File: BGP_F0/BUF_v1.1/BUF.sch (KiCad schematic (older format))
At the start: 34 parts, among them P1 CONN_01X02, P2 CONN_01X02, P3 CONN_01X03, P4 CONN_01X02, P5 Conn_01x06, P6 Conn_01x05, P7 CONN_01X02, Q1 2N5457, Q2 2N5457, U1 MC33178

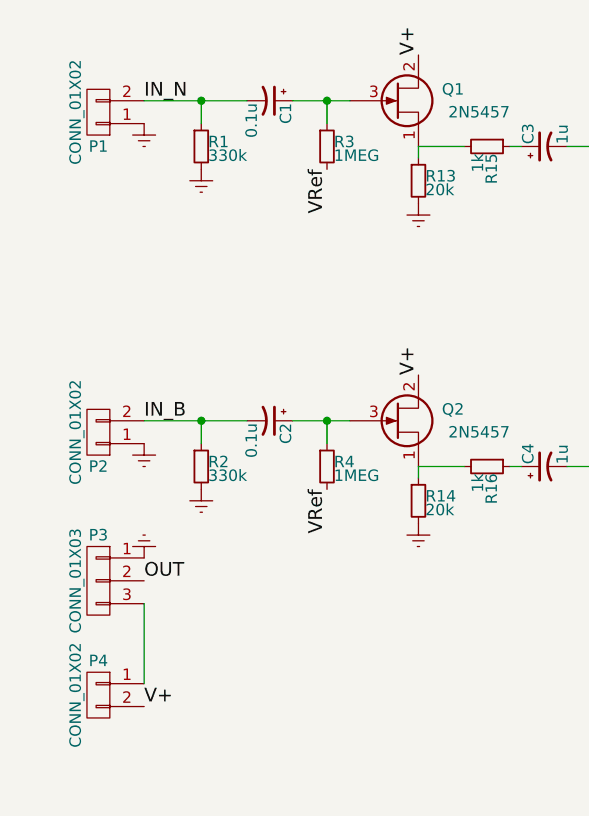
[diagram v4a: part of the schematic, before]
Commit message: F0 - BUF JFET bypass caps at i/p
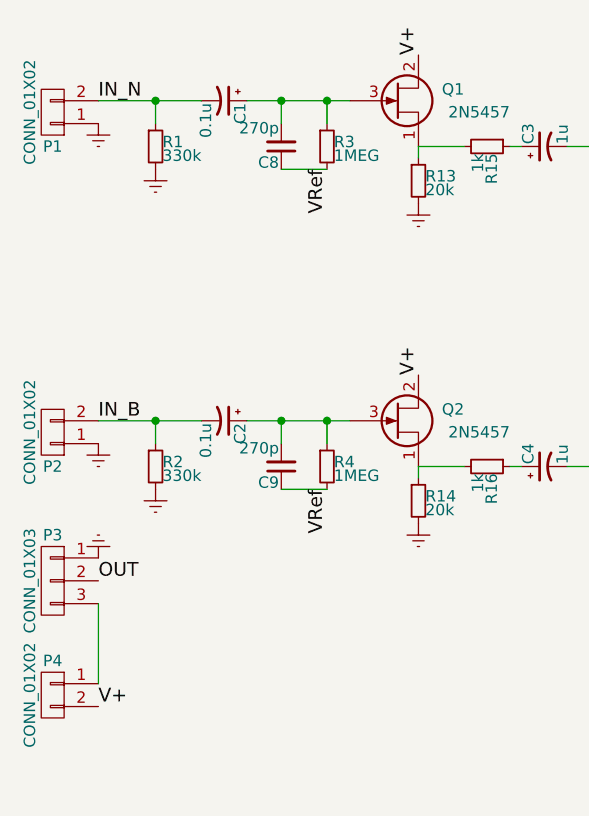
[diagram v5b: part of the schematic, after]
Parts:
- added C8, C9: 270p, Capacitors_SMD:C_0603, symbol C_Small
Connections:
- net VRef: now also C8.1, C9.1
- net at C1.1, Q1.3 (G), R3.1: now also C8.2
- net at C2.1, Q2.3 (G), R4.1: now also C9.2
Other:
- moved on the sheet: C1, C2, P1, P2, P3, P4, R1, R2
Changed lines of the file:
@@
 L R_Small R1
 U 1 1 5A65126F
-P 2850 2700
-F 0 "R1" H 2880 2720 50  0000 L CNN
-F 1 "330k" H 2880 2660 50  0000 L CNN
-F 2 "Resistors_SMD:R_0603" H 2850 2700 50  0001 C CNN
-F 3 "" H 2850 2700 50  0000 C CNN
-	1    2850 2700
+P 2650 2700
+F 0 "R1" H 2680 2720 50  0000 L CNN
+F 1 "330k" H 2680 2660 50  0000 L CNN
+F 2 "Resistors_SMD:R_0603" H 2650 2700 50  0001 C CNN
+F 3 "" H 2650 2700 50  0000 C CNN
+	1    2650 2700
 	1    0    0    -1
 $EndComp
@@
 L Earth #PWR01
 U 1 1 5A651373
-P 2850 2800
-F 0 "#PWR01" H 2850 2550 50  0001 C CNN
-F 1 "Earth" H 2850 2650 50  0001 C CNN
-F 2 "" H 2850 2800 50  0000 C CNN
-F 3 "" H 2850 2800 50  0000 C CNN
-	1    2850 2800
+P 2650 2800
+F 0 "#PWR01" H 2650 2550 50  0001 C CNN
+F 1 "Earth" H 2650 2650 50  0001 C CNN
+F 2 "" H 2650 2800 50  0000 C CNN
+F 3 "" H 2650 2800 50  0000 C CNN
+	1    2650 2800
 	1    0    0    -1
 $EndComp
@@
 L R_Small R2
 U 1 1 5A653A92
-P 2850 4100
-F 0 "R2" H 2880 4120 50  0000 L CNN
-F 1 "330k" H 2880 4060 50  0000 L CNN
-F 2 "Resistors_SMD:R_0603" H 2850 4100 50  0001 C CNN
-F 3 "" H 2850 4100 50  0000 C CNN
-	1    2850 4100
+P 2650 4100
+F 0 "R2" H 2680 4120 50  0000 L CNN
+F 1 "330k" H 2680 4060 50  0000 L CNN
+F 2 "Resistors_SMD:R_0603" H 2650 4100 50  0001 C CNN
+F 3 "" H 2650 4100 50  0000 C CNN
+	1    2650 4100
 	1    0    0    -1
 $EndComp
@@
 Text Label 6400 3300 0    60   ~ 0
 IN_EQ
-Text Label 2600 3900 0    60   ~ 0
+Text Label 2400 3900 0    60   ~ 0
 IN_B
 Text Label 8350 3550 2    60   ~ 0
@@
 Text Label 8350 4600 2    60   ~ 0
 V+
-Text Label 2600 5150 0    60   ~ 0
+Text Label 2400 5150 0    60   ~ 0
 V+
-Text Label 2600 4600 0    60   ~ 0
+Text Label 2400 4600 0    60   ~ 0
 OUT
 $Comp
 L Earth #PWR07
 U 1 1 5A658545
-P 2600 4000
-F 0 "#PWR07" H 2600 3750 50  0001 C CNN
-F 1 "Earth" H 2600 3850 50  0001 C CNN
-F 2 "" H 2600 4000 50  0000 C CNN
-F 3 "" H 2600 4000 50  0000 C CNN
-	1    2600 4000
+P 2400 4000
+F 0 "#PWR07" H 2400 3750 50  0001 C CNN
+F 1 "Earth" H 2400 3850 50  0001 C CNN
+F 2 "" H 2400 4000 50  0000 C CNN
+F 3 "" H 2400 4000 50  0000 C CNN
+	1    2400 4000
 	1    0    0    -1
 $EndComp
@@
 L Earth #PWR08
 U 1 1 5A6585B9
-P 2600 2600
-F 0 "#PWR08" H 2600 2350 50  0001 C CNN
-F 1 "Earth" H 2600 2450 50  0001 C CNN
-F 2 "" H 2600 2600 50  0000 C CNN
-F 3 "" H 2600 2600 50  0000 C CNN
-	1    2600 2600
-	1    0    0    -1
-$EndComp
-Text Label 2600 2500 0    60   ~ 0
+P 2400 2600
+F 0 "#PWR08" H 2400 2350 50  0001 C CNN
+F 1 "Earth" H 2400 2450 50  0001 C CNN
+F 2 "" H 2400 2600 50  0000 C CNN
+F 3 "" H 2400 2600 50  0000 C CNN
+	1    2400 2600
+	1    0    0    -1
+$EndComp
+Text Label 2400 2500 0    60   ~ 0
 IN_N
 Text Label 6100 5100 0    60   ~ 0
@@
 Wire Wire Line
 	4850 5150 4850 4800
-Connection ~ 2850 3900
-Connection ~ 2850 2500
-Wire Wire Line
-	2600 5050 2600 4700
+Connection ~ 2650 3900
+Connection ~ 2650 2500
+Wire Wire Line
+	2400 5050 2400 4700
 Wire Wire Line
 	7100 3300 6750 3300
@@
 	3800 4150 3800 4100
 Wire Wire Line
-	2850 3900 2850 4000
-Wire Wire Line
-	2600 3900 3050 3900
+	2650 3900 2650 4000
+Wire Wire Line
+	2400 3900 2850 3900
 Connection ~ 3400 3900
 Wire Wire Line
 	3400 3900 3400 4000
 Wire Wire Line
-	2850 2500 2850 2600
-Wire Wire Line
-	2600 2500 3050 2500
+	2650 2500 2650 2600
+Wire Wire Line
+	2400 2500 2850 2500
 Connection ~ 3400 2500
 Wire Wire Line
@@
 	3800 2750 3800 2700
 Wire Wire Line
-	3500 2500 3250 2500
-Wire Wire Line
-	3500 3900 3250 3900
+	3050 2500 3500 2500
+Wire Wire Line
+	3050 3900 3500 3900
 $Comp
 L Earth #PWR010
 U 1 1 5A65837A
-P 2600 4500
-F 0 "#PWR010" H 2600 4250 50  0001 C CNN
-F 1 "Earth" H 2600 4350 50  0001 C CNN
-F 2 "" H 2600 4500 50  0000 C CNN
-F 3 "" H 2600 4500 50  0000 C CNN
-	1    2600 4500
+P 2400 4500
+F 0 "#PWR010" H 2400 4250 50  0001 C CNN
+F 1 "Earth" H 2400 4350 50  0001 C CNN
+F 2 "" H 2400 4500 50  0000 C CNN
+F 3 "" H 2400 4500 50  0000 C CNN
+	1    2400 4500
 	-1   0    0    1
 $EndComp
@@
 L Earth #PWR011
 U 1 1 5A653A9E
-P 2850 4200
-F 0 "#PWR011" H 2850 3950 50  0001 C CNN
-F 1 "Earth" H 2850 4050 50  0001 C CNN
-F 2 "" H 2850 4200 50  0000 C CNN
-F 3 "" H 2850 4200 50  0000 C CNN
-	1    2850 4200
+P 2650 4200
+F 0 "#PWR011" H 2650 3950 50  0001 C CNN
+F 1 "Earth" H 2650 4050 50  0001 C CNN
+F 2 "" H 2650 4200 50  0000 C CNN
+F 3 "" H 2650 4200 50  0000 C CNN
+	1    2650 4200
 	1    0    0    -1
 $EndComp
@@
 L CP1_Small C1
 U 1 1 5A79331B
-P 3150 2500
-F 0 "C1" H 3160 2570 50  0000 L CNN
-F 1 "0.1u" H 3160 2420 50  0000 L CNN
-F 2 "Capacitors_Tantalum_SMD:TantalC_SizeR_EIA-2012" H 3150 2500 50  0001 C CNN
-F 3 "" H 3150 2500 50  0000 C CNN
-	1    3150 2500
+P 2950 2500
+F 0 "C1" H 2960 2570 50  0000 L CNN
+F 1 "0.1u" H 2960 2420 50  0000 L CNN
+F 2 "Capacitors_Tantalum_SMD:TantalC_SizeR_EIA-2012" H 2950 2500 50  0001 C CNN
+F 3 "" H 2950 2500 50  0000 C CNN
+	1    2950 2500
 	0    1    1    0
 $EndComp
@@
 L CP1_Small C2
 U 1 1 5A793406
-P 3150 3900
-F 0 "C2" H 3160 3970 50  0000 L CNN
-F 1 "0.1u" H 3160 3820 50  0000 L CNN
-F 2 "Capacitors_Tantalum_SMD:TantalC_SizeR_EIA-2012" H 3150 3900 50  0001 C CNN
-F 3 "" H 3150 3900 50  0000 C CNN
-	1    3150 3900
+P 2950 3900
+F 0 "C2" H 2960 3970 50  0000 L CNN
+F 1 "0.1u" H 2960 3820 50  0000 L CNN
+F 2 "Capacitors_Tantalum_SMD:TantalC_SizeR_EIA-2012" H 2950 3900 50  0001 C CNN
+F 3 "" H 2950 3900 50  0000 C CNN
+	1    2950 3900
 	0    1    1    0
 $EndComp
@@
 L CONN_01X03 P3
 U 1 1 5A657F5B
-P 2400 4600
-F 0 "P3" H 2400 4800 50  0000 C CNN
-F 1 "CONN_01X03" V 2500 4600 50  0000 C CNN
-F 2 "Terminal_Blocks:TerminalBlock_Pheonix_MPT-2.54mm_3pol" H 2400 4600 50  0001 C CNN
-F 3 "" H 2400 4600 50  0000 C CNN
-	1    2400 4600
+P 2200 4600
+F 0 "P3" H 2200 4800 50  0000 C CNN
+F 1 "CONN_01X03" V 2300 4600 50  0000 C CNN
+F 2 "Terminal_Blocks:TerminalBlock_Pheonix_MPT-2.54mm_3pol" H 2200 4600 50  0001 C CNN
+F 3 "" H 2200 4600 50  0000 C CNN
+	1    2200 4600
 	-1   0    0    -1
 $EndComp
@@
 L CONN_01X02 P4
 U 1 1 5A658137
-P 2400 5100
-F 0 "P4" H 2400 5250 50  0000 C CNN
-F 1 "CONN_01X02" V 2500 5100 50  0000 C CNN
-F 2 "Terminal_Blocks:TerminalBlock_Pheonix_MPT-2.54mm_2pol" H 2400 5100 50  0001 C CNN
-F 3 "" H 2400 5100 50  0000 C CNN
-	1    2400 5100
+P 2200 5100
+F 0 "P4" H 2200 5250 50  0000 C CNN
+F 1 "CONN_01X02" V 2300 5100 50  0000 C CNN
+F 2 "Terminal_Blocks:TerminalBlock_Pheonix_MPT-2.54mm_2pol" H 2200 5100 50  0001 C CNN
+F 3 "" H 2200 5100 50  0000 C CNN
+	1    2200 5100
 	-1   0    0    -1
 $EndComp
@@
 L CONN_01X02 P2
 U 1 1 5A656625
-P 2400 3950
-F 0 "P2" H 2400 4100 50  0000 C CNN
-F 1 "CONN_01X02" V 2500 3950 50  0000 C CNN
-F 2 "Terminal_Blocks:TerminalBlock_Pheonix_MPT-2.54mm_2pol" H 2400 3950 50  0001 C CNN
-F 3 "" H 2400 3950 50  0000 C CNN
-	1    2400 3950
+P 2200 3950
+F 0 "P2" H 2200 4100 50  0000 C CNN
+F 1 "CONN_01X02" V 2300 3950 50  0000 C CNN
+F 2 "Terminal_Blocks:TerminalBlock_Pheonix_MPT-2.54mm_2pol" H 2200 3950 50  0001 C CNN
+F 3 "" H 2200 3950 50  0000 C CNN
+	1    2200 3950
 	-1   0    0    1
 $EndComp
@@
 L CONN_01X02 P1
 U 1 1 5A65640A
-P 2400 2550
-F 0 "P1" H 2400 2700 50  0000 C CNN
-F 1 "CONN_01X02" V 2500 2550 50  0000 C CNN
-F 2 "Terminal_Blocks:TerminalBlock_Pheonix_MPT-2.54mm_2pol" H 2400 2550 50  0001 C CNN
-F 3 "" H 2400 2550 50  0000 C CNN
-	1    2400 2550
+P 2200 2550
+F 0 "P1" H 2200 2700 50  0000 C CNN
+F 1 "CONN_01X02" V 2300 2550 50  0000 C CNN
+F 2 "Terminal_Blocks:TerminalBlock_Pheonix_MPT-2.54mm_2pol" H 2200 2550 50  0001 C CNN
+F 3 "" H 2200 2550 50  0000 C CNN
+	1    2200 2550
 	-1   0    0    1
 $EndComp
@@
 	1    0    0    -1
 $EndComp
+$Comp
+L C_Small C8
+U 1 1 5AF7B3CC
+P 3200 2700
+F 0 "C8" H 3210 2770 50  0000 L CNN
+F 1 "270p" H 3210 2620 50  0000 L CNN
+F 2 "Capacitors_SMD:C_0603" H 3200 2700 50  0001 C CNN
+F 3 "" H 3200 2700 50  0000 C CNN
+	1    3200 2700
+	-1   0    0    1
+$EndComp
+$Comp
+L C_Small C9
+U 1 1 5AF7B618
+P 3200 4100
+F 0 "C9" H 3210 4170 50  0000 L CNN
+F 1 "270p" H 3210 4020 50  0000 L CNN
+F 2 "Capacitors_SMD:C_0603" H 3200 4100 50  0001 C CNN
+F 3 "" H 3200 4100 50  0000 C CNN
+	1    3200 4100
+	-1   0    0    1
+$EndComp
+Wire Wire Line
+	3200 4200 3400 4200
+Wire Wire Line
+	3200 4000 3200 3900
+Connection ~ 3200 3900
+Wire Wire Line
+	3200 2800 3400 2800
+Wire Wire Line
+	3200 2600 3200 2500
+Connection ~ 3200 2500
 $EndSCHEMATC

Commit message: Various
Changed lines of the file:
@@
 Text Label 7650 3300 0    60   ~ 0
 OUT
-Text Label 6400 3300 0    60   ~ 0
+Text Label 6650 3300 2    60   ~ 0
 IN_EQ
 Text Label 2400 3900 0    60   ~ 0

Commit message: Various
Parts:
- R5, R6: value 4.7k -> 100k
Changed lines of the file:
@@
 P 5200 2800
 F 0 "R5" H 5230 2820 50  0000 L CNN
-F 1 "4.7k" H 5230 2760 50  0000 L CNN
+F 1 "100k" H 5230 2760 50  0000 L CNN
 F 2 "Resistors_SMD:R_0603" H 5200 2800 50  0001 C CNN
 F 3 "" H 5200 2800 50  0000 C CNN
@@
 P 5200 3200
 F 0 "R6" H 5230 3220 50  0000 L CNN
-F 1 "4.7k" H 5230 3160 50  0000 L CNN
+F 1 "100k" H 5230 3160 50  0000 L CNN
 F 2 "Resistors_SMD:R_0603" H 5200 3200 50  0001 C CNN
 F 3 "" H 5200 3200 50  0000 C CNN
